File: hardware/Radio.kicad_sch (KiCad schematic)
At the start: 0 parts

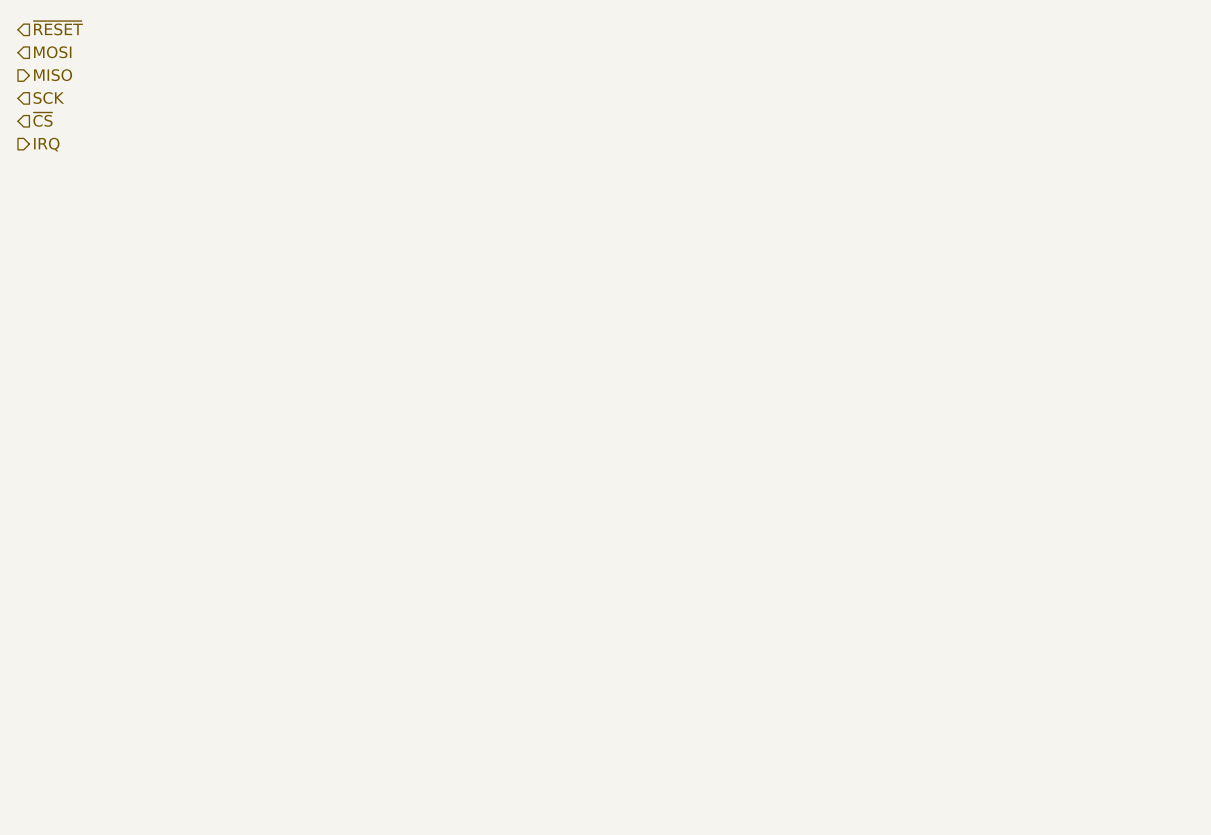
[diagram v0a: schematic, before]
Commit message: Schematic and layout Progress
Signed-off-by: Connor Rigby <connorr@hey.com>
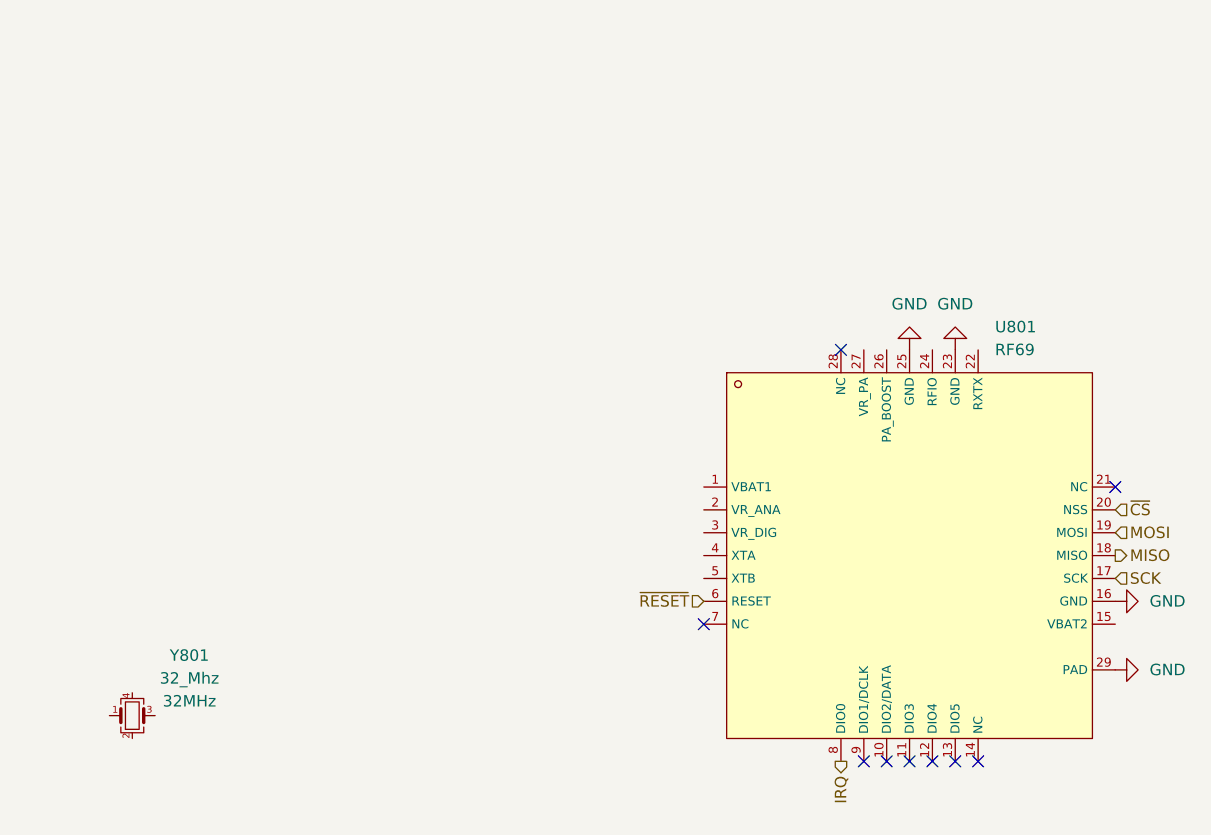
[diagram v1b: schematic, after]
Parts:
- added U801: RF69, Package_DFN_QFN:QFN-28-1EP_5x5mm_P0.5mm_EP3.75x3.75mm_ThermalVias, symbol LCSC_RF_Transciever_ICs:RF69
- added Y801: 32_Mhz, Crystal:Crystal_SMD_3225-4Pin_3.2x2.5mm, symbol LCSC_Crystal:32_Mhz
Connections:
- net IRQ: now also U801.8 (DIO0)
- net MISO: now also U801.18 (MISO)
- net MOSI: now also U801.19 (MOSI)
- net SCK: now also U801.17 (SCK)
- net ~{CS}: now also U801.20 (NSS)
- net ~{RESET}: now also U801.6 (RESET)
- new net GND: U801.16 (GND), U801.23 (GND), U801.25 (GND), U801.29 (PAD)
- no-connect marks 0 -> 9
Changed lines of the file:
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@@
-(kicad_sch (version 20211123) (generator eeschema)
+(kicad_sch (version 20230121) (generator eeschema)
   (paper "A4")
-  (hierarchical_label "~{CS}" (shape input) (at 25.4 35.56 0)
-    (effects (font (size 1.27 1.27)) (justify left))
-  )
-  (hierarchical_label "IRQ" (shape output) (at 25.4 38.1 0)
-    (effects (font (size 1.27 1.27)) (justify left))
-  )
-  (hierarchical_label "MISO" (shape output) (at 25.4 30.48 0)
-    (effects (font (size 1.27 1.27)) (justify left))
-  )
-  (hierarchical_label "MOSI" (shape input) (at 25.4 27.94 0)
-    (effects (font (size 1.27 1.27)) (justify left))
-  )
-  (hierarchical_label "SCK" (shape input) (at 25.4 33.02 0)
-    (effects (font (size 1.27 1.27)) (justify left))
-  )
-  (hierarchical_label "~{RESET}" (shape input) (at 25.4 25.4 0)
-    (effects (font (size 1.27 1.27)) (justify left))
+  (no_connect (at 121.92 106.68))
+  (no_connect (at 132.08 106.68))
+  (no_connect (at 124.46 106.68))
+  (no_connect (at 119.38 106.68))
+  (no_connect (at 147.32 76.2))
+  (no_connect (at 116.84 60.96))
+  (no_connect (at 129.54 106.68))
+  (no_connect (at 101.6 91.44))
+  (no_connect (at 127 106.68))
+  (hierarchical_label "~{CS}" (shape input) (at 147.32 78.74 0) (fields_autoplaced)
+    (effects (font (size 1.27 1.27)) (justify left))
+  )
+  (hierarchical_label "IRQ" (shape output) (at 116.84 106.68 270) (fields_autoplaced)
+    (effects (font (size 1.27 1.27)) (justify right))
+  )
+  (hierarchical_label "MISO" (shape output) (at 147.32 83.82 0) (fields_autoplaced)
+    (effects (font (size 1.27 1.27)) (justify left))
+  )
+  (hierarchical_label "MOSI" (shape input) (at 147.32 81.28 0) (fields_autoplaced)
+    (effects (font (size 1.27 1.27)) (justify left))
+  )
+  (hierarchical_label "SCK" (shape input) (at 147.32 86.36 0) (fields_autoplaced)
+    (effects (font (size 1.27 1.27)) (justify left))
+  )
+  (hierarchical_label "~{RESET}" (shape input) (at 101.6 88.9 180) (fields_autoplaced)
+    (effects (font (size 1.27 1.27)) (justify right))
+  )
+  (symbol (lib_id "LCSC_Crystal:32_Mhz") (at 38.1 101.6 0) (unit 1)
+    (in_bom yes) (on_board yes) (dnp no) (fields_autoplaced)
+    (property "Reference" "Y801" (at 44.45 94.9198 0)
+      (effects (font (size 1.27 1.27)))
+    )
+    (property "Value" "32_Mhz" (at 44.45 97.4598 0)
+      (effects (font (size 1.27 1.27)))
+    )
+    (property "Footprint" "Crystal:Crystal_SMD_3225-4Pin_3.2x2.5mm" (at 38.1 101.6 0)
+      (effects (font (size 1.27 1.27)) hide)
+    )
+    (property "Datasheet" "https://datasheet.lcsc.com/lcsc/2208241730_TAE-Zhejiang-Abel-Elec-TAXM32M4RLBCDT2T_C5143379.pdf" (at 38.1 101.6 0)
+      (effects (font (size 1.27 1.27)) hide)
+    )
+    (property "MPN" "TAXM32M4RLBCDT2T" (at 38.1 101.6 0)
+      (effects (font (size 1.27 1.27)) hide)
+    )
+    (property "LCSC" "C5143379" (at 38.1 101.6 0)
+      (effects (font (size 1.27 1.27)) hide)
+    )
+    (property "Frequency" "32MHz" (at 44.45 99.9998 0)
+      (effects (font (size 1.27 1.27)))
+    )
+    (pin "1")
+    (pin "2")
+    (pin "3")
+    (pin "4")
+    (instances
+      (project "underglow2"
+        (path "/dcbdf88a-d6ac-4b1d-9514-0b0ce113d90b/bab1dc88-b79a-454f-b699-1d1b3e7eefdd"
+          (reference "Y801") (unit 1)
+        )
+      )
+    )
+  )
+  (symbol (lib_id "power:GND") (at 129.54 60.96 180) (unit 1)
+    (in_bom yes) (on_board yes) (dnp no) (fields_autoplaced)
+    (property "Reference" "#PWR0164" (at 129.54 54.61 0)
+      (effects (font (size 1.27 1.27)) hide)
+    )
+    (property "Value" "GND" (at 129.54 55.88 0)
+      (effects (font (size 1.27 1.27)))
+    )
+    (property "Footprint" "" (at 129.54 60.96 0)
+      (effects (font (size 1.27 1.27)) hide)
+    )
+    (property "Datasheet" "" (at 129.54 60.96 0)
+      (effects (font (size 1.27 1.27)) hide)
+    )
+    (pin "1")
+    (instances
+      (project "underglow2"
+        (path "/dcbdf88a-d6ac-4b1d-9514-0b0ce113d90b/bab1dc88-b79a-454f-b699-1d1b3e7eefdd"
+          (reference "#PWR0164") (unit 1)
+        )
+      )
+    )
+  )
+  (symbol (lib_id "power:GND") (at 124.46 60.96 180) (unit 1)
+    (in_bom yes) (on_board yes) (dnp no) (fields_autoplaced)
+    (property "Reference" "#PWR0165" (at 124.46 54.61 0)
+      (effects (font (size 1.27 1.27)) hide)
+    )
+    (property "Value" "GND" (at 124.46 55.88 0)
+      (effects (font (size 1.27 1.27)))
+    )
+    (property "Footprint" "" (at 124.46 60.96 0)
+      (effects (font (size 1.27 1.27)) hide)
+    )
+    (property "Datasheet" "" (at 124.46 60.96 0)
+      (effects (font (size 1.27 1.27)) hide)
+    )
+    (pin "1")
+    (instances
+      (project "underglow2"
+        (path "/dcbdf88a-d6ac-4b1d-9514-0b0ce113d90b/bab1dc88-b79a-454f-b699-1d1b3e7eefdd"
+          (reference "#PWR0165") (unit 1)
+        )
+      )
+    )
+  )
+  (symbol (lib_id "power:GND") (at 147.32 88.9 90) (unit 1)
+    (in_bom yes) (on_board yes) (dnp no) (fields_autoplaced)
+    (property "Reference" "#PWR0162" (at 153.67 88.9 0)
+      (effects (font (size 1.27 1.27)) hide)
+    )
+    (property "Value" "GND" (at 151.13 88.8999 90)
+      (effects (font (size 1.27 1.27)) (justify right))
+    )
+    (property "Footprint" "" (at 147.32 88.9 0)
+      (effects (font (size 1.27 1.27)) hide)
+    )
+    (property "Datasheet" "" (at 147.32 88.9 0)
+      (effects (font (size 1.27 1.27)) hide)
+    )
+    (pin "1")
+    (instances
+      (project "underglow2"
+        (path "/dcbdf88a-d6ac-4b1d-9514-0b0ce113d90b/bab1dc88-b79a-454f-b699-1d1b3e7eefdd"
+          (reference "#PWR0162") (unit 1)
+        )
+      )
+    )
+  )
+  (symbol (lib_id "LCSC_RF_Transciever_ICs:RF69") (at 124.46 83.82 0) (unit 1)
+    (in_bom yes) (on_board yes) (dnp no) (fields_autoplaced)
+    (property "Reference" "U801" (at 133.9509 58.42 0)
+      (effects (font (size 1.27 1.27)) (justify left))
+    )
+    (property "Value" "RF69" (at 133.9509 60.96 0)
+      (effects (font (size 1.27 1.27)) (justify left))
+    )
+    (property "Footprint" "Package_DFN_QFN:QFN-28-1EP_5x5mm_P0.5mm_EP3.75x3.75mm_ThermalVias" (at 140.97 58.42 0)
+      (effects (font (size 1.27 1.27)) hide)
+    )
+    (property "Datasheet" "https://datasheet.lcsc.com/lcsc/1811142212_HopeRF-Micro-electronics-RF69_C77220.pdf" (at 140.97 58.42 0)
+      (effects (font (size 1.27 1.27)) hide)
+    )
+    (property "MPN" "RF69" (at 124.46 83.82 0)
+      (effects (font (size 1.27 1.27)) hide)
+    )
+    (property "LCSC" "C77220" (at 124.46 83.82 0)
+      (effects (font (size 1.27 1.27)) hide)
+    )
+    (pin "1")
+    (pin "10")
+    (pin "11")
+    (pin "12")
+    (pin "13")
+    (pin "14")
+    (pin "15")
+    (pin "16")
+    (pin "17")
+    (pin "18")
+    (pin "19")
+    (pin "2")
+    (pin "20")
+    (pin "21")
+    (pin "22")
+    (pin "23")
+    (pin "24")
+    (pin "25")
+    (pin "26")
+    (pin "27")
+    (pin "28")
+    (pin "29")
+    (pin "3")
+    (pin "4")
+    (pin "5")
+    (pin "6")
+    (pin "7")
+    (pin "8")
+    (pin "9")
+    (instances
+      (project "underglow2"
+        (path "/dcbdf88a-d6ac-4b1d-9514-0b0ce113d90b/bab1dc88-b79a-454f-b699-1d1b3e7eefdd"
+          (reference "U801") (unit 1)
+        )
+      )
+    )
+  )
+  (symbol (lib_id "power:GND") (at 147.32 96.52 90) (unit 1)
+    (in_bom yes) (on_board yes) (dnp no) (fields_autoplaced)
+    (property "Reference" "#PWR0163" (at 153.67 96.52 0)
+      (effects (font (size 1.27 1.27)) hide)
+    )
+    (property "Value" "GND" (at 151.13 96.5199 90)
+      (effects (font (size 1.27 1.27)) (justify right))
+    )
+    (property "Footprint" "" (at 147.32 96.52 0)
+      (effects (font (size 1.27 1.27)) hide)
+    )
+    (property "Datasheet" "" (at 147.32 96.52 0)
+      (effects (font (size 1.27 1.27)) hide)
+    )
+    (pin "1")
+    (instances
+      (project "underglow2"
+        (path "/dcbdf88a-d6ac-4b1d-9514-0b0ce113d90b/bab1dc88-b79a-454f-b699-1d1b3e7eefdd"
+          (reference "#PWR0163") (unit 1)
+        )
+      )
+    )
   )
 )

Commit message: Layout updates
Signed-off-by: Connor Rigby <connorr@hey.com>
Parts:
- added C801, C813: C_0402_DNP, Capacitor_SMD:C_0402_1005Metric, symbol LCSC_Capacitor:C_0402_DNP
- added C810, C811, C812, C815: C_0402_100nf_X7R, Capacitor_SMD:C_0402_1005Metric, symbol LCSC_Capacitor:C_0402_100nf_X7R
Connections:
- net GND: now also Y801.2, Y801.4, C801.2, C810.2, C811.2, C812.2, C813.2, C815.2
- net XTA: now reaches Y801.1
- net XTA: now also U801.4 (XTA), C813.1
- net XTB: now reaches Y801.3
- net XTB: now also U801.5 (XTB), C801.1
- net +3.3V: now reaches U801.1 (VBAT1)
- net +3.3V: now also U801.15 (VBAT2), C810.1, C815.1
- net VR_ANA: now reaches U801.2 (VR_ANA)
- net VR_ANA: now also C811.1
- net VR_DIG: now reaches U801.3 (VR_DIG)
- net VR_DIG: now also C812.1
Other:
- moved on the sheet: U801, Y801

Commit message: Update layout
Signed-off-by: Connor Rigby <connorr@hey.com>
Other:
- moved on the sheet: C801, C810, C811, C812, C813, C815, U801, Y801

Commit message: layout updates
Signed-off-by: Connor Rigby <connorr@hey.com>
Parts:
- added ANT801: BWSMA-KE-P001, LCSC_Antenna:SMA-SMD_BWSMA-KE-P001, symbol LCSC_Antenna:BWSMA-KE-P001
- added C801: C_0805_10u_X5R, Capacitor_SMD:C_0805_2012Metric, symbol LCSC_Capacitor:C_0805_10u_X5R
- added C802, C803, C804, C805, C806, C807, C808, C809, C816, C817, C818, C819, C820, C821, C822, C823, C824, C825, C826, C827: C_0402_DNP, Capacitor_SMD:C_0402_1005Metric, symbol LCSC_Capacitor:C_0402_DNP
- added L801, L802, L803, L804, L805, L806, L807, L808: L_0402_DNP, Inductor_SMD:L_0402_1005Metric, symbol LCSC_Inductor:L_0402_DNP
- added Q305: BCX56, Package_TO_SOT_SMD:SOT-89-3, symbol LCSC_Transistor:BCX56
- added R801, R803, R804: R_0402_DNP, Resistor_SMD:R_0402_1005Metric, symbol LCSC_Resistor:R_0402_DNP
- added R802: R_0402_10k, Resistor_SMD:R_0402_1005Metric, symbol LCSC_Resistor:R_0402_10k
- added U802: AS193-73LF, Package_TO_SOT_SMD:SOT-363_SC-70-6, symbol LCSC_RF_Transciever_ICs:AS193-73LF
- renumbered C801 to C814
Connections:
- net +3.3V: now also C801.1, R801.1, R802.1
- net GND: now also ANT801.1, ANT801.2, ANT801.3, ANT801.4, C801.2, C802.2, C804.2, C807.2, C808.2, C809.2, C816.2, C817.2, C820.2, C822.2, C826.1, C827.1, Q305.3 (E), U802.2 (GND)
- net ~{RESET}: now also R801.2
- net RXTX: now reaches U801.22 (RXTX)
- net RXTX: now also R803.1, U802.6 (V1)
- net RF_IO: now reaches U801.24 (RFIO)
- net RF_IO: now also L805.1
- net PA_BOOST: now reaches U801.26 (PA_BOOST)
- net PA_BOOST: now also L804.2
- net VR_PA: now reaches U801.27 (VR_PA)
- net VR_PA: now also C808.1, C809.1, C816.1, L803.2, L806.2
- new net J1: C825.1, U802.5 (J1)
- new net J2: C823.2, U802.1 (J2)
- new net J3: C824.2, U802.3 (J3)
- new net PA_BOOST_MATCH: C806.2, C807.1, L803.1, L804.1
- new net PA_BOOST_RF: C805.2, C806.1, L802.2
- new net RF69_ANTENNA: ANT801.5, C827.2, R804.2
- new net RF69_ANT_MATCH: C825.2, C826.2, R804.1
- new net RF_IO_MATCH: C817.1, C818.1, L805.2, L806.1
- new net RF_IO_RF: C818.2, C819.1, L807.1
- new net RXTX_INV: Q305.1 (B), R803.2
- new net RX_ANT: C821.2, C822.1, C823.1, L808.2
- new net RX_ANT_MATCH: C819.2, C820.1, C821.1, L807.2, L808.1
- new net TX_ANT: C802.1, C803.1, C824.1, L801.1
- new net TX_ANT_MATCH: C803.2, C804.1, C805.1, L801.2, L802.1
- new net ~{RXTX}: Q305.2 (C), R802.2, U802.4 (V2)
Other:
- note added: "100pf"
- note added: "RX"
- note added: "RXTX is HIGH in TX"
- note added: "TX"
- note added: "| V1 | V2 | J1-J2 | J1-J3 | | LO | HI | inser | isola | | HI | LO | isola | inser |"
- moved on the sheet: C810, C811, C812, C813, C814, C815, U801, Y801
